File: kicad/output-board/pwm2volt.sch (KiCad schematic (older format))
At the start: 30 parts, among them U11 LM324

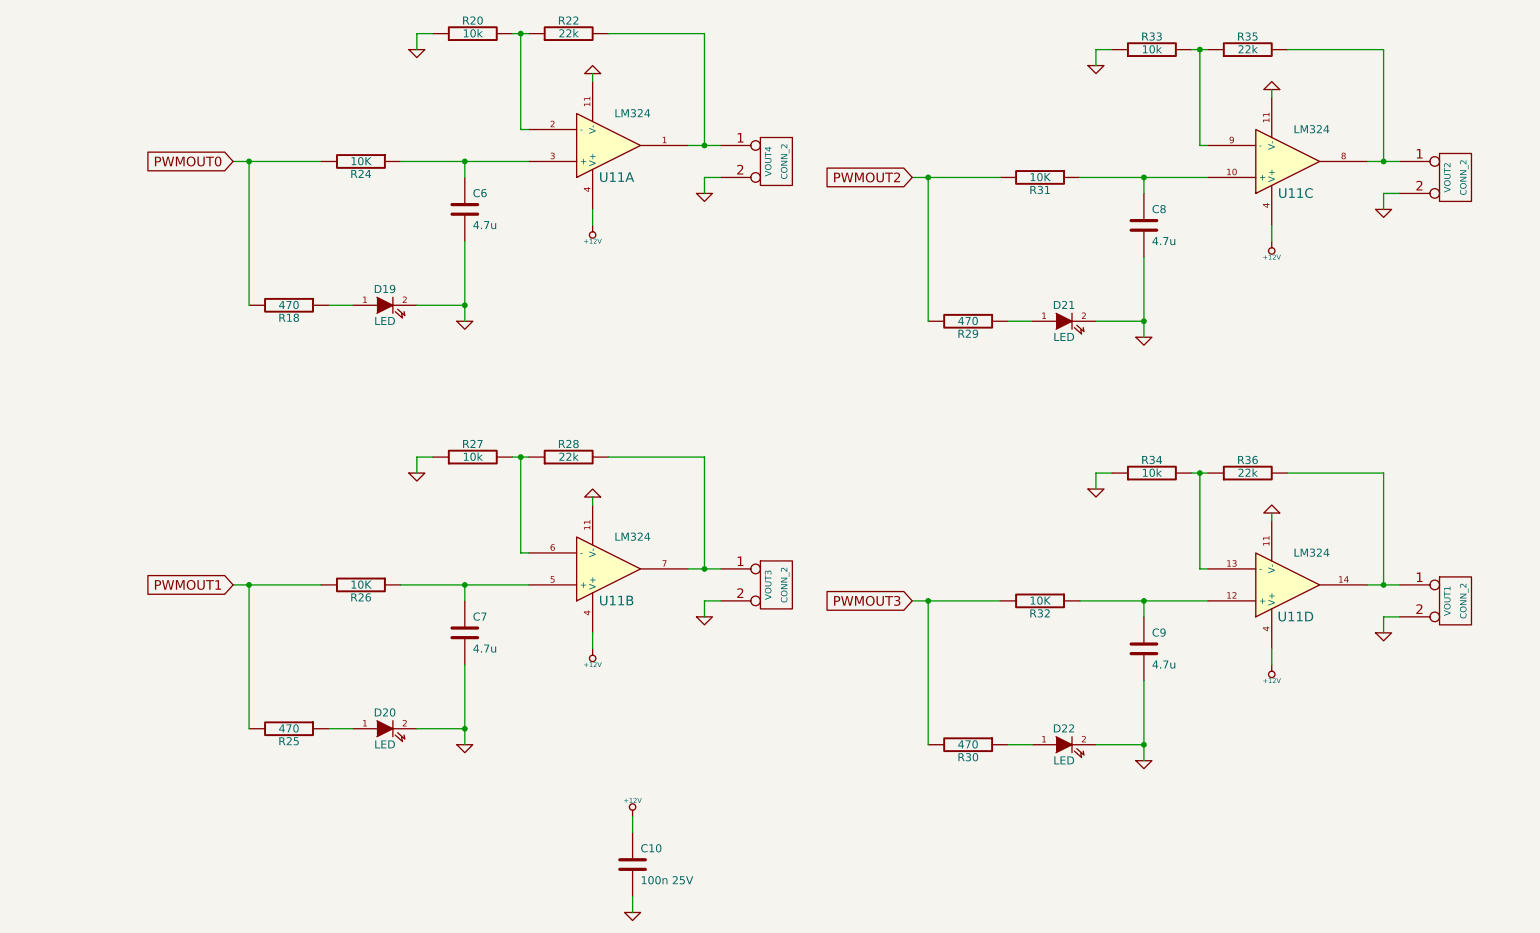
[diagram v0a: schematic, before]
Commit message: Placed non-inverting buffer between panStamp and op-amp.
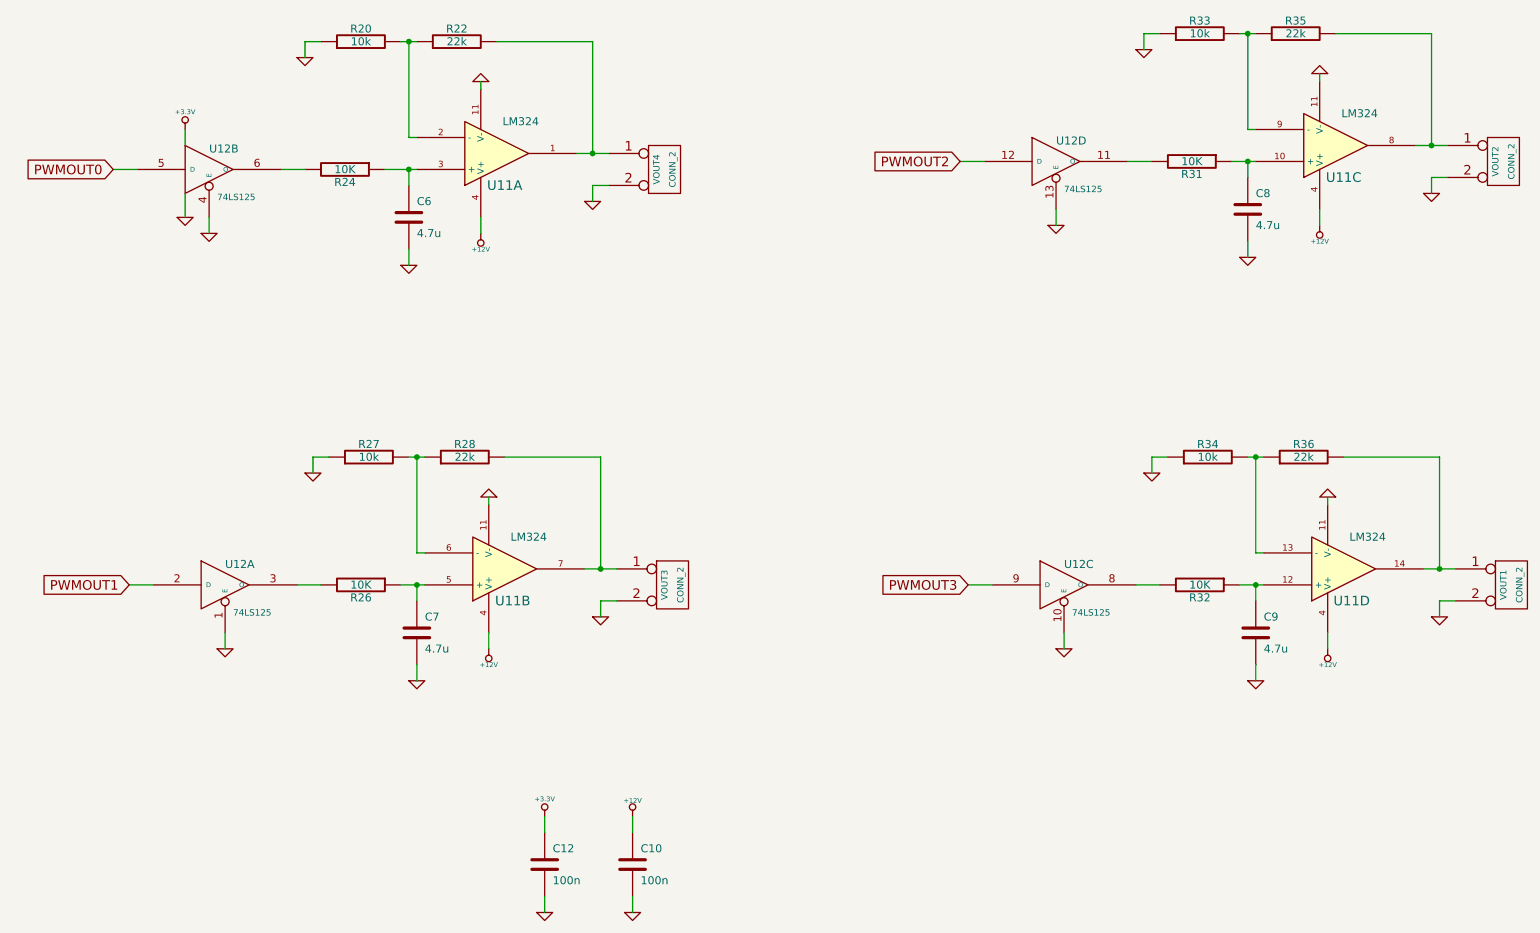
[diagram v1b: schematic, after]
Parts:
- removed D19, D20, D21, D22: LED, SM0603_POL, symbol LED
- removed R18, R25, R29, R30: 470, SM0603S, symbol R
- added C12: 100n, SM0603S, symbol C
- added U12: 74LS125, SO14E, symbol 74LS125
- C10: value 100n 25V -> 100n
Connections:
- net GND: now also C12.2, U12.1 (E), U12.10 (E), U12.13 (E), U12.4 (E), U12.7 (GND), U12.7 (GND), U12.7 (GND), U12.7 (GND)
- net PWMOUT0: now also U12.5 (D); no longer R24.2
- net PWMOUT1: now also U12.2 (D); no longer R26.2
- net PWMOUT2: now also U12.12 (D); no longer R31.2
- net PWMOUT3: now also U12.9 (D); no longer R32.2
- new net: R24.2, U12.6 (O)
- new net: R26.2, U12.3 (O)
- new net: R32.2, U12.8 (O)
- new net: R31.2, U12.11 (O)
- new net +3.3V: C12.1, U12.14 (VCC), U12.14 (VCC), U12.14 (VCC), U12.14 (VCC)
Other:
- moved on the sheet: C6, C7, C8, C9, R20, R22, R24, R27, R28, R31, R32, R33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

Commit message: Buffer removed in pwm2volt circuit
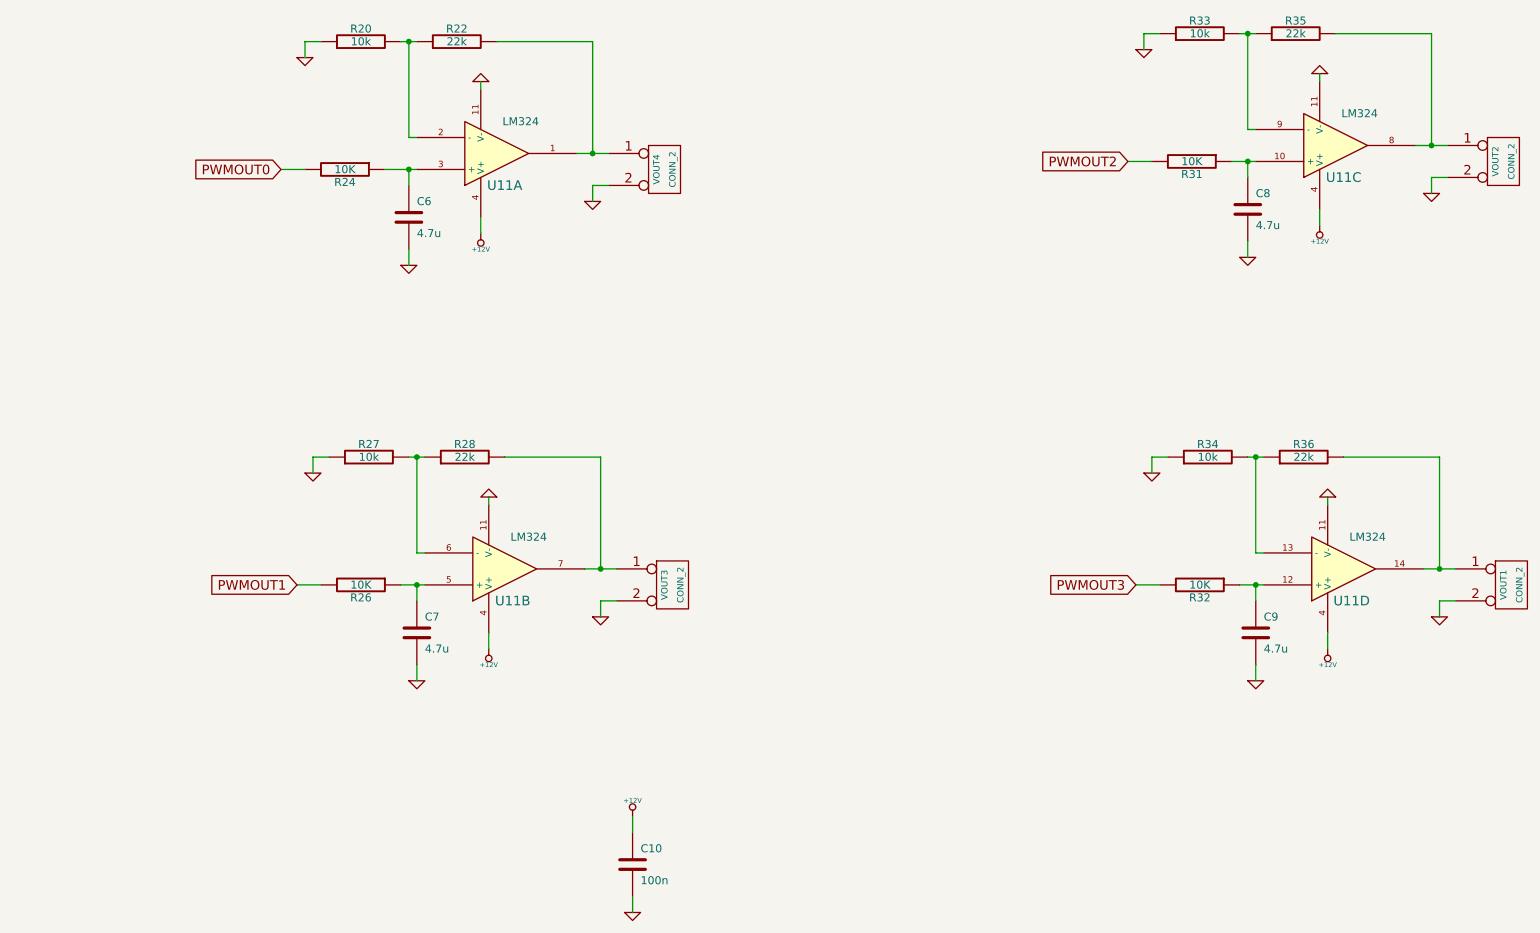
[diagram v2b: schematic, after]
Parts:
- removed C12: 100n, SM0603S, symbol C
- removed U12: 74LS125, SO14E, symbol 74LS125
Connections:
- net PWMOUT0: now also R24.2
- net PWMOUT1: now also R26.2
- net PWMOUT2: now also R31.2
- net PWMOUT3: now also R32.2
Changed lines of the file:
@@
-EESchema Schematic File Version 2  date Tue 24 Jul 2012 05:50:09 PM CEST
+EESchema Schematic File Version 2  date Mon 06 Aug 2012 06:14:15 PM CEST
 LIBS:power
 LIBS:device
@@
 LIBS:toshiba
 LIBS:output-board-cache
-EELAYER 24  0
+EELAYER 25  0
 EELAYER END
 $Descr A4 11700 8267
 Sheet 2 3
 Title "panStamp relay and 0-10V output board"
-Date "24 jul 2012"
-Rev "01"
+Date "6 aug 2012"
+Rev "1.2"
 Comp "www.panstamp.com"
 Comment1 "PWM to 0-10V conversion"
@@
 $EndDescr
 Wire Wire Line
-	4350 6200 4350 6100
-Wire Wire Line
-	7600 4950 7600 5050
-Wire Wire Line
 	8800 5150 8800 5250
 Wire Wire Line
@@
 	8650 2000 8800 2000
 Wire Wire Line
-	6950 2000 7100 2000
+	8000 2000 8150 2000
 Wire Wire Line
 	3550 5150 3550 5250
@@
 	3450 4650 3600 4650
 Wire Wire Line
-	1750 4650 1900 4650
+	2800 4650 2950 4650
 Wire Wire Line
 	3500 2050 3500 2150
-Wire Wire Line
-	2100 1800 2100 1900
-Wire Wire Line
-	2250 2350 2250 2450
-Wire Wire Line
-	2850 2050 2700 2050
 Wire Wire Line
 	4900 6200 4900 6100
@@
 	4900 6600 4900 6700
 Wire Wire Line
-	1800 2050 1650 2050
-Wire Wire Line
-	2100 2200 2100 2350
+	2850 2050 2700 2050
 Wire Wire Line
 	3500 2550 3500 2650
@@
 Connection ~ 3500 2050
 Wire Wire Line
-	2800 4650 2950 4650
-Wire Wire Line
 	3550 4750 3550 4650
 Connection ~ 3550 4650
 Wire Wire Line
-	2350 4950 2350 5050
-Wire Wire Line
-	8000 2000 8150 2000
-Wire Wire Line
 	8750 2100 8750 2000
 Connection ~ 8750 2000
 Wire Wire Line
-	7550 2300 7550 2400
-Wire Wire Line
 	8800 4750 8800 4650
 Connection ~ 8800 4650
 Wire Wire Line
 	8200 4650 8050 4650
-Wire Wire Line
-	7150 4650 7000 4650
-Wire Wire Line
-	4350 6600 4350 6700
-$Comp
-L +3.3V #PWR019
-U 1 1 500EC2E3
-P 4350 6100
-F 0 "#PWR019" H 4350 6060 30  0001 C CNN
-F 1 "+3.3V" H 4350 6210 30  0000 C CNN
-	1    4350 6100
-	1    0    0    -1
-$EndComp
-$Comp
-L C C12
-U 1 1 500EC2D9
-P 4350 6400
-F 0 "C12" H 4400 6500 50  0000 L CNN
-F 1 "100n" H 4400 6300 50  0000 L CNN
-F 2 "SM0603S" H 4350 6400 60  0001 C CNN
-	1    4350 6400
-	1    0    0    -1
-$EndComp
 $Comp
 L GND #PWR020
-U 1 1 500EC2D7
-P 4350 6700
-F 0 "#PWR020" H 4350 6700 30  0001 C CNN
-F 1 "GND" H 4350 6630 30  0001 C CNN
-	1    4350 6700
-	1    0    0    -1
-$EndComp
-$Comp
-L GND #PWR021
-U 1 1 500EBFCF
-P 7600 5050
-F 0 "#PWR021" H 7600 5050 30  0001 C CNN
-F 1 "GND" H 7600 4980 30  0001 C CNN
-	1    7600 5050
-	1    0    0    -1
-$EndComp
-$Comp
-L 74LS125 U12
-U 3 1 500EBFA8
-P 7600 4650
-F 0 "U12" H 7600 4750 50  0000 L BNN
-F 1 "74LS125" H 7650 4500 40  0000 L TNN
-F 2 "SO14E" H 7600 4650 60  0001 C CNN
-	3    7600 4650
-	1    0    0    -1
-$EndComp
-$Comp
-L GND #PWR022
-U 1 1 500EBF68
-P 7550 2400
-F 0 "#PWR022" H 7550 2400 30  0001 C CNN
-F 1 "GND" H 7550 2330 30  0001 C CNN
-	1    7550 2400
-	1    0    0    -1
-$EndComp
-$Comp
-L 74LS125 U12
-U 4 1 500EBF2F
-P 7550 2000
-F 0 "U12" H 7550 2100 50  0000 L BNN
-F 1 "74LS125" H 7600 1850 40  0000 L TNN
-F 2 "SO14E" H 7550 2000 60  0001 C CNN
-	4    7550 2000
-	1    0    0    -1
-$EndComp
-$Comp
-L GND #PWR023
-U 1 1 500EBF09
-P 2350 5050
-F 0 "#PWR023" H 2350 5050 30  0001 C CNN
-F 1 "GND" H 2350 4980 30  0001 C CNN
-	1    2350 5050
-	1    0    0    -1
-$EndComp
-$Comp
-L 74LS125 U12
-U 1 1 500EBE47
-P 2350 4650
-F 0 "U12" H 2350 4750 50  0000 L BNN
-F 1 "74LS125" H 2400 4500 40  0000 L TNN
-F 2 "SO14E" H 2350 4650 60  0001 C CNN
-	1    2350 4650
-	1    0    0    -1
-$EndComp
-$Comp
-L +3.3V #PWR024
-U 1 1 500EBE0A
-P 2100 1800
-F 0 "#PWR024" H 2100 1760 30  0001 C CNN
-F 1 "+3.3V" H 2100 1910 30  0000 C CNN
-	1    2100 1800
-	1    0    0    -1
-$EndComp
-$Comp
-L GND #PWR025
-U 1 1 500EBD31
-P 2100 2350
-F 0 "#PWR025" H 2100 2350 30  0001 C CNN
-F 1 "GND" H 2100 2280 30  0001 C CNN
-	1    2100 2350
-	1    0    0    -1
-$EndComp
-$Comp
-L GND #PWR026
-U 1 1 500EBCD3
-P 2250 2450
-F 0 "#PWR026" H 2250 2450 30  0001 C CNN
-F 1 "GND" H 2250 2380 30  0001 C CNN
-	1    2250 2450
-	1    0    0    -1
-$EndComp
-$Comp
-L 74LS125 U12
-U 2 1 500EBC43
-P 2250 2050
-F 0 "U12" H 2250 2150 50  0000 L BNN
-F 1 "74LS125" H 2300 1900 40  0000 L TNN
-F 2 "SO14E" H 2250 2050 60  0001 C CNN
-	2    2250 2050
-	1    0    0    -1
-$EndComp
-$Comp
-L GND #PWR027
 U 1 1 4FD8C2A0
 P 4900 6700
-F 0 "#PWR027" H 4900 6700 30  0001 C CNN
+F 0 "#PWR020" H 4900 6700 30  0001 C CNN
 F 1 "GND" H 4900 6630 30  0001 C CNN
 	1    4900 6700
@@
 $EndComp
 $Comp
-L +12V #PWR028
+L +12V #PWR021
 U 1 1 4FD8C29B
 P 4900 6100
-F 0 "#PWR028" H 4900 6050 20  0001 C CNN
+F 0 "#PWR021" H 4900 6050 20  0001 C CNN
 F 1 "+12V" H 4900 6200 30  0000 C CNN
 	1    4900 6100
@@
 	1    0    0    -1
 $EndComp
-Text GLabel 7000 4650 0    60   Input ~ 0
+Text GLabel 8050 4650 0    60   Input ~ 0
 PWMOUT3
-Text GLabel 6950 2000 0    60   Input ~ 0
+Text GLabel 8000 2000 0    60   Input ~ 0
 PWMOUT2
-Text GLabel 1750 4650 0    60   Input ~ 0
+Text GLabel 2800 4650 0    60   Input ~ 0
 PWMOUT1
-Text GLabel 1650 2050 0    60   Input ~ 0
+Text GLabel 2700 2050 0    60   Input ~ 0
 PWMOUT0
 $Comp
@@
 $EndComp
 $Comp
-L GND #PWR029
+L GND #PWR022
 U 1 1 4FCC6A9F
 P 8750 2600
-F 0 "#PWR029" H 8750 2600 30  0001 C CNN
+F 0 "#PWR022" H 8750 2600 30  0001 C CNN
 F 1 "GND" H 8750 2530 30  0001 C CNN
 	1    8750 2600
@@
 $EndComp
 $Comp
-L GND #PWR030
+L GND #PWR023
 U 1 1 4FCC6A99
 P 8100 1300
-F 0 "#PWR030" H 8100 1300 30  0001 C CNN
+F 0 "#PWR023" H 8100 1300 30  0001 C CNN
 F 1 "GND" H 8100 1230 30  0001 C CNN
 	1    8100 1300
@@
 $EndComp
 $Comp
-L +12V #PWR031
+L +12V #PWR024
 U 1 1 4FCC6A97
 P 9200 2400
-F 0 "#PWR031" H 9200 2350 20  0001 C CNN
+F 0 "#PWR024" H 9200 2350 20  0001 C CNN
 F 1 "+12V" H 9200 2500 30  0000 C CNN
 	1    9200 2400
@@
 $EndComp
 $Comp
-L GND #PWR032
+L GND #PWR025
 U 1 1 4FCC6A95
 P 9200 1450
-F 0 "#PWR032" H 9200 1450 30  0001 C CNN
+F 0 "#PWR025" H 9200 1450 30  0001 C CNN
 F 1 "GND" H 9200 1380 30  0001 C CNN
 	1    9200 1450
@@
 $EndComp
 $Comp
-L GND #PWR033
+L GND #PWR026
 U 1 1 4FCC6A94
 P 9900 2200
-F 0 "#PWR033" H 9900 2200 30  0001 C CNN
+F 0 "#PWR026" H 9900 2200 30  0001 C CNN
 F 1 "GND" H 9900 2130 30  0001 C CNN
 	1    9900 2200
@@
 $EndComp
 $Comp
-L GND #PWR034
+L GND #PWR027
 U 1 1 4FCC6A93
 P 9950 4850
-F 0 "#PWR034" H 9950 4850 30  0001 C CNN
+F 0 "#PWR027" H 9950 4850 30  0001 C CNN
 F 1 "GND" H 9950 4780 30  0001 C CNN
 	1    9950 4850
@@
 $EndComp
 $Comp
-L GND #PWR035
+L GND #PWR028
 U 1 1 4FCC6A92
 P 9250 4100
-F 0 "#PWR035" H 9250 4100 30  0001 C CNN
+F 0 "#PWR028" H 9250 4100 30  0001 C CNN
 F 1 "GND" H 9250 4030 30  0001 C CNN
 	1    9250 4100
@@
 $EndComp
 $Comp
-L +12V #PWR036
+L +12V #PWR029
 U 1 1 4FCC6A90
 P 9250 5050
-F 0 "#PWR036" H 9250 5000 20  0001 C CNN
+F 0 "#PWR029" H 9250 5000 20  0001 C CNN
 F 1 "+12V" H 9250 5150 30  0000 C CNN
 	1    9250 5050
@@
 $EndComp
 $Comp
-L GND #PWR037
+L GND #PWR030
 U 1 1 4FCC6A8E
 P 8150 3950
-F 0 "#PWR037" H 8150 3950 30  0001 C CNN
+F 0 "#PWR030" H 8150 3950 30  0001 C CNN
 F 1 "GND" H 8150 3880 30  0001 C CNN
 	1    8150 3950
@@
 $EndComp
 $Comp
-L GND #PWR038
+L GND #PWR031
 U 1 1 4FCC6A88
 P 8800 5250
-F 0 "#PWR038" H 8800 5250 30  0001 C CNN
+F 0 "#PWR031" H 8800 5250 30  0001 C CNN
 F 1 "GND" H 8800 5180 30  0001 C CNN
 	1    8800 5250
@@
 $EndComp
 $Comp
-L GND #PWR039
+L GND #PWR032
 U 1 1 4FCC6A85
 P 3550 5250
-F 0 "#PWR039" H 3550 5250 30  0001 C CNN
+F 0 "#PWR032" H 3550 5250 30  0001 C CNN
 F 1 "GND" H 3550 5180 30  0001 C CNN
 	1    3550 5250
@@
 $EndComp
 $Comp
-L GND #PWR040
+L GND #PWR033
 U 1 1 4FCC6A7F
 P 2900 3950
-F 0 "#PWR040" H 2900 3950 30  0001 C CNN
+F 0 "#PWR033" H 2900 3950 30  0001 C CNN
 F 1 "GND" H 2900 3880 30  0001 C CNN
 	1    2900 3950
@@
 $EndComp
 $Comp
-L +12V #PWR041
+L +12V #PWR034
 U 1 1 4FCC6A7D
 P 4000 5050
-F 0 "#PWR041" H 4000 5000 20  0001 C CNN
+F 0 "#PWR034" H 4000 5000 20  0001 C CNN
 F 1 "+12V" H 4000 5150 30  0000 C CNN
 	1    4000 5050
@@
 $EndComp
 $Comp
-L GND #PWR042
+L GND #PWR035
 U 1 1 4FCC6A7B
 P 4000 4100
-F 0 "#PWR042" H 4000 4100 30  0001 C CNN
+F 0 "#PWR035" H 4000 4100 30  0001 C CNN
 F 1 "GND" H 4000 4030 30  0001 C CNN
 	1    4000 4100
@@
 $EndComp
 $Comp
-L GND #PWR043
+L GND #PWR036
 U 1 1 4FCC6A7A
 P 4700 4850
-F 0 "#PWR043" H 4700 4850 30  0001 C CNN
+F 0 "#PWR036" H 4700 4850 30  0001 C CNN
 F 1 "GND" H 4700 4780 30  0001 C CNN
 	1    4700 4850
@@
 $EndComp
 $Comp
-L GND #PWR044
+L GND #PWR037
 U 1 1 4FCB8BCC
 P 4650 2250
-F 0 "#PWR044" H 4650 2250 30  0001 C CNN
+F 0 "#PWR037" H 4650 2250 30  0001 C CNN
 F 1 "GND" H 4650 2180 30  0001 C CNN
 	1    4650 2250
@@
 $EndComp
 $Comp
-L GND #PWR045
+L GND #PWR038
 U 1 1 4FCB8BC4
 P 3950 1500
-F 0 "#PWR045" H 3950 1500 30  0001 C CNN
+F 0 "#PWR038" H 3950 1500 30  0001 C CNN
 F 1 "GND" H 3950 1430 30  0001 C CNN
 	1    3950 1500
@@
 $EndComp
 $Comp
-L +12V #PWR046
+L +12V #PWR039
 U 1 1 4FAD2D39
 P 3950 2450
-F 0 "#PWR046" H 3950 2400 20  0001 C CNN
+F 0 "#PWR039" H 3950 2400 20  0001 C CNN
 F 1 "+12V" H 3950 2550 30  0000 C CNN
 	1    3950 2450
@@
 $EndComp
 $Comp
-L GND #PWR047
+L GND #PWR040
 U 1 1 4FAD1E62
 P 2850 1350
-F 0 "#PWR047" H 2850 1350 30  0001 C CNN
+F 0 "#PWR040" H 2850 1350 30  0001 C CNN
 F 1 "GND" H 2850 1280 30  0001 C CNN
 	1    2850 1350
@@
 $EndComp
 $Comp
-L GND #PWR048
+L GND #PWR041
 U 1 1 4FAD1BEC
 P 3500 2650
-F 0 "#PWR048" H 3500 2650 30  0001 C CNN
+F 0 "#PWR041" H 3500 2650 30  0001 C CNN
 F 1 "GND" H 3500 2580 30  0001 C CNN
 	1    3500 2650
